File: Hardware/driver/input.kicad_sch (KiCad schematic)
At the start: 63 parts, among them J301 1017526, Q301 IXTH80N075L2, Q302 IXTH80N075L2, U301 MCP3421A2T-ECH, U302 MCP3421A1T-ECH, U303 DAC60501Z, U304 DAC60501Z, U305 DS18B20, U306 DS18B20, U307 MCP3421A3T-ECH, U308 OPA2388, U309 OPA2388, U310 LM431SC, U311 LM431SC

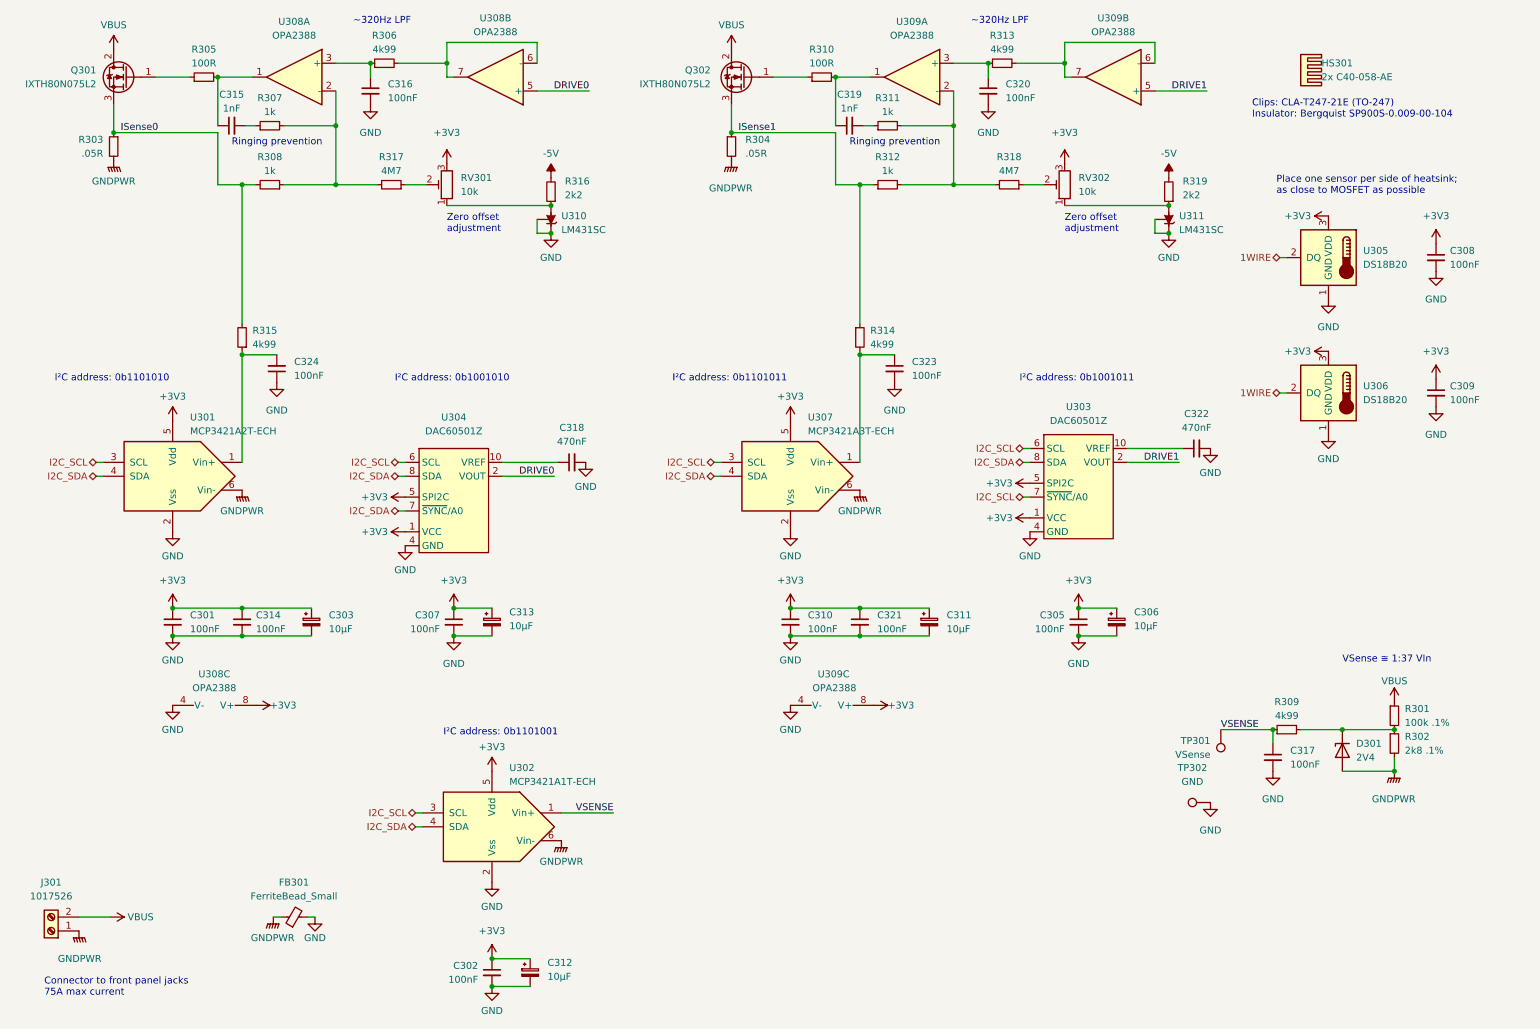
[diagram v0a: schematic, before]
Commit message: Start work on remote VSense; driver board tweaks
- Use the DAC reference as the positive end of the null adjustment
  trimmers, rather than the +3V3 supply; this should make the adjustment
  actually useful and persistent rather than relying on the relationship
  between the 3V3 rail and the DAC's internal reference.

- Moved the 1Wire controller slightly to allow relocating the zero
  offset trimmer for the first channel

- Start work on remote VSense

  This works by selecting between either voltage sensing at the source
  terminals, or an external sense input connected to another set of
  terminals. These are switched by a latching relay (as to provide
  satisfying clicky noises) and then go into an op amp working as a
  differential amplifier; it performs a 50:1 gain (obviating the need
  for resistor dividers, and providing greater accuracy) and that then
  goes into the measurement ADC as normal.

  We have to still figure out how to drive the relay (probably just an
  IO expander?) and place those components on the board.
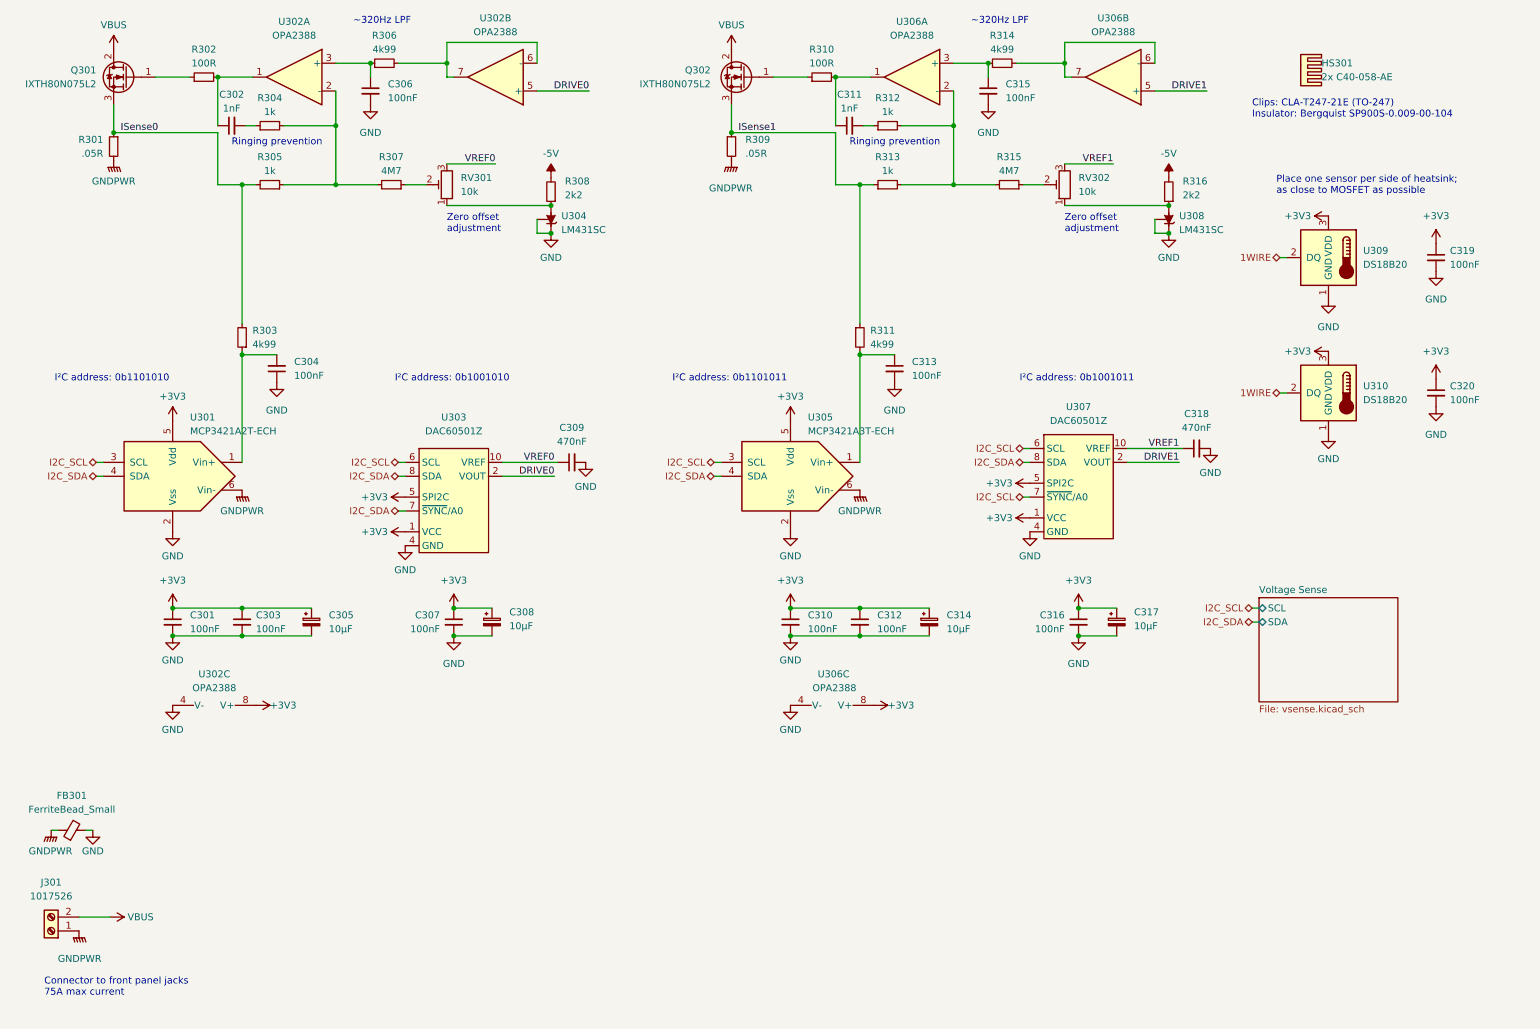
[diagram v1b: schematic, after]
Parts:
- removed C302, C317: 100nF, Capacitor_SMD:C_0805_2012Metric_Pad1.18x1.45mm_HandSolder, symbol Device:C_Small
- removed C312: 10µF, Capacitor_Tantalum_SMD:CP_EIA-3216-18_Kemet-A_Pad1.58x1.35mm_HandSolder, symbol Device:C_Polarized_Small
- removed D301: 2V4, Diode_SMD:D_MiniMELF_Handsoldering, symbol Device:D_Zener
- removed R301: 100k .1%, Resistor_SMD:R_1206_3216Metric_Pad1.30x1.75mm_HandSolder, symbol Device:R_Small
- removed R302: 2k8 .1%, Resistor_SMD:R_1206_3216Metric_Pad1.30x1.75mm_HandSolder, symbol Device:R_Small
- removed R309: 4k99, Resistor_SMD:R_0805_2012Metric_Pad1.20x1.40mm_HandSolder, symbol Device:R_Small
- removed TP301: VSense, TestPoint:TestPoint_Keystone_5000-5004_Miniature, symbol Connector:TestPoint
- removed TP302: GND, TestPoint:TestPoint_Keystone_5000-5004_Miniature, symbol Connector:TestPoint
- removed U302: MCP3421A1T-ECH, Package_TO_SOT_SMD:SOT-23-6_Handsoldering, symbol Analog_ADC:MCP3421A0T-ECH
- renumbered C315 to C302, C314 to C303, C324 to C304, C303 to C305, C316 to C306, C313 to C308, C318 to C309, C319 to C311, C321 to C312, C323 to C313, C311 to C314, C320 to C315, C305 to C316, C306 to C317, C322 to C318, C308 to C319, C309 to C320, R303 to R301, R305 to R302, R315 to R303, R307 to R304, R308 to R305, R317 to R307, R316 to R308, R304 to R309, R314 to R311, R311 to R312, R312 to R313, R313 to R314, R318 to R315, R319 to R316, U308 to U302, U304 to U303, U310 to U304, U307 to U305, U309 to U306, U303 to U307, U311 to U308, U305 to U309, U306 to U310
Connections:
- net +3V3: no longer RV301.3, RV302.3
- net VREF1: now reaches C318.1, U307.10 (VREF)
- net VREF1: now also RV302.3
- net VREF0: now reaches C309.1, U303.10 (VREF)
- net VREF0: now also RV301.3
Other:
- added sheet Voltage Sense (vsense.kicad_sch)
- note removed: "I²C address: 0b1101001"
- note removed: "VSense ≅ 1:37 VIn"
- moved on the sheet: FB301

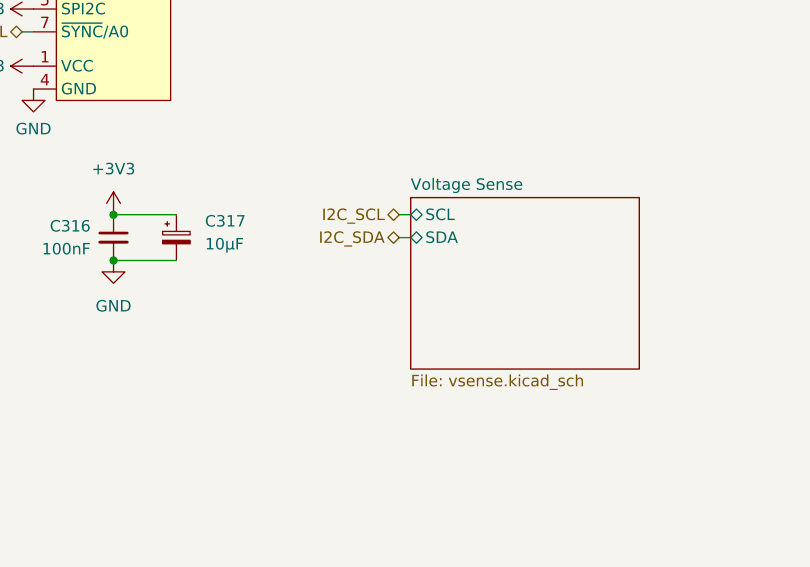
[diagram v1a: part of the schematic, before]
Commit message: Finished remote VSense support
- Laid out the VSense amp and analog-to-digital converter, as well as
  added an I2C IO expander to handle driving the latching relay to
  switch between internal and external sense.

  Also moved the input connector and some of the analog parts around to
  accomodate this all.

- Status indicator (with an extra GPIO on the IO expander) in the form
  of a single LED
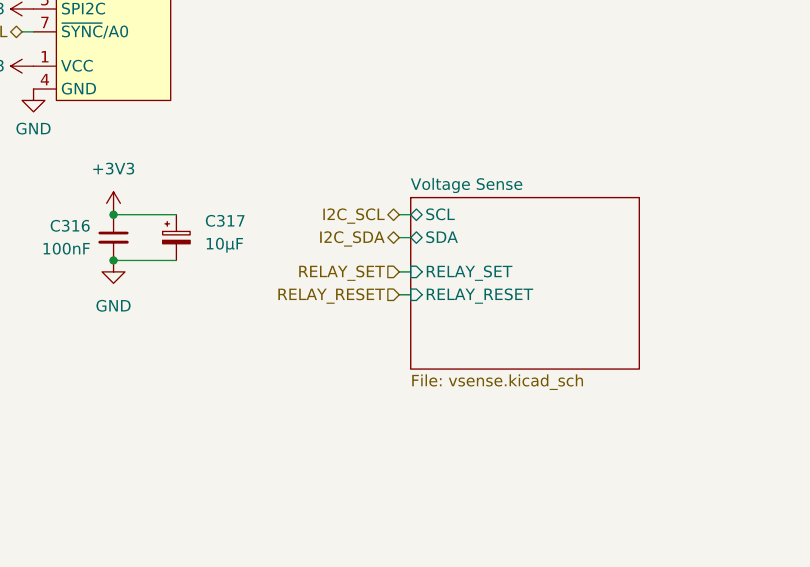
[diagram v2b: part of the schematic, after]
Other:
- sheet Voltage Sense ports: added RELAY_RESET, RELAY_SET; removed none
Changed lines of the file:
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@@
     (comment 1 "Isense options: .1R (Johanson Dielectrics RHXH3N000R1F4), .05R (Ohmite AP101 R05 J)")
     (comment 2 "Drive DACs (U303, U304) can be DAC70501Z or DAC80501Z")
+    (comment 3 "RV301, RV302 adjust current null offset")
   )
   (junction (at 155.575 127.635) (diameter 0) (color 0 0 0 0)
@@
     (stroke (width 0) (type default) (color 0 0 0 0))
   )
+  (wire (pts (xy 240.03 131.445) (xy 241.3 131.445))
+    (stroke (width 0) (type default) (color 0 0 0 0))
+  )
   (wire (pts (xy 111.76 53.975) (xy 109.22 53.975))
     (stroke (width 0) (type default) (color 0 0 0 0))
@@
   )
   (wire (pts (xy 163.83 35.56) (xy 163.83 45.085))
+    (stroke (width 0) (type default) (color 0 0 0 0))
+  )
+  (wire (pts (xy 240.03 128.905) (xy 241.3 128.905))
     (stroke (width 0) (type default) (color 0 0 0 0))
   )
@@
     (effects (font (size 1.27 1.27)) (justify right))
   )
+  (hierarchical_label "RELAY_RESET" (shape input) (at 240.03 131.445 180)
+    (effects (font (size 1.27 1.27)) (justify right))
+  )
   (hierarchical_label "I2C_SCL" (shape bidirectional) (at 240.03 122.555 180)
     (effects (font (size 1.27 1.27)) (justify right))
@@
   )
   (hierarchical_label "I2C_SCL" (shape bidirectional) (at 141.605 95.885 180)
+    (effects (font (size 1.27 1.27)) (justify right))
+  )
+  (hierarchical_label "RELAY_SET" (shape input) (at 240.03 128.905 180)
     (effects (font (size 1.27 1.27)) (justify right))
   )
@@
       (effects (font (size 1.27 1.27)) (justify left))
     )
+    (pin "RELAY_SET" input (at 241.3 128.905 180)
+      (effects (font (size 1.27 1.27)) (justify left))
+    )
+    (pin "RELAY_RESET" input (at 241.3 131.445 180)
+      (effects (font (size 1.27 1.27)) (justify left))
+    )

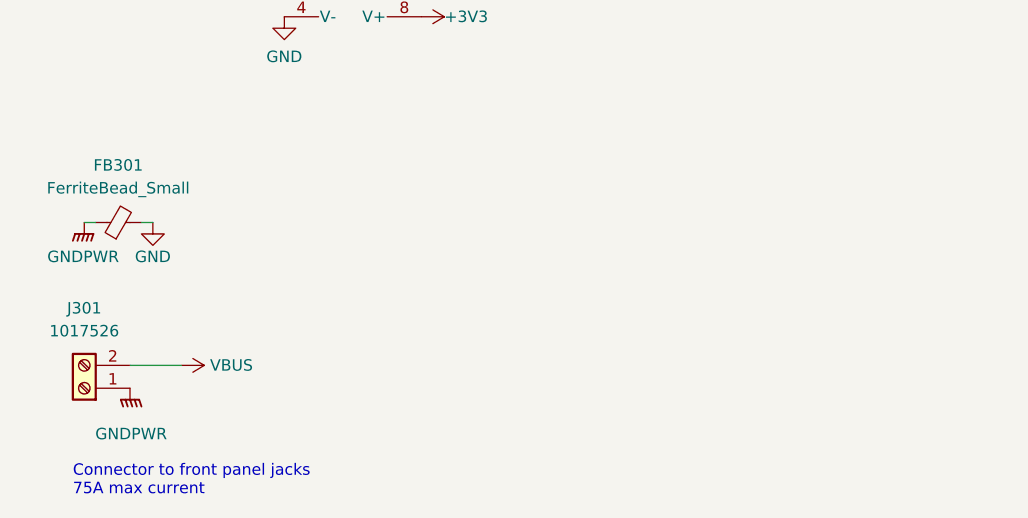
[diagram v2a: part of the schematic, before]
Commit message: Driver input protection; heatsink footprint tweaks
- Updated the footprint for the heatsink on the driver board to include
  a 3D model. Also fixed it… the distances were kind of out of whack and
  it would never have really fit

- Added a reverse polarity protection diode to the input; it gets its
  own cute little heatsink

- Minor movement to better accomodate a fan. A 20mm fan will likely
  interfere with the input connector (it might be worth switching to a
  different kind, or just soldering the connections altogether: spade
  terminals seem like a good choice for high current) and be very tight
  against the input diode's heatsink. We'll try with a 10mm fan and see
  if that's enough airflow.
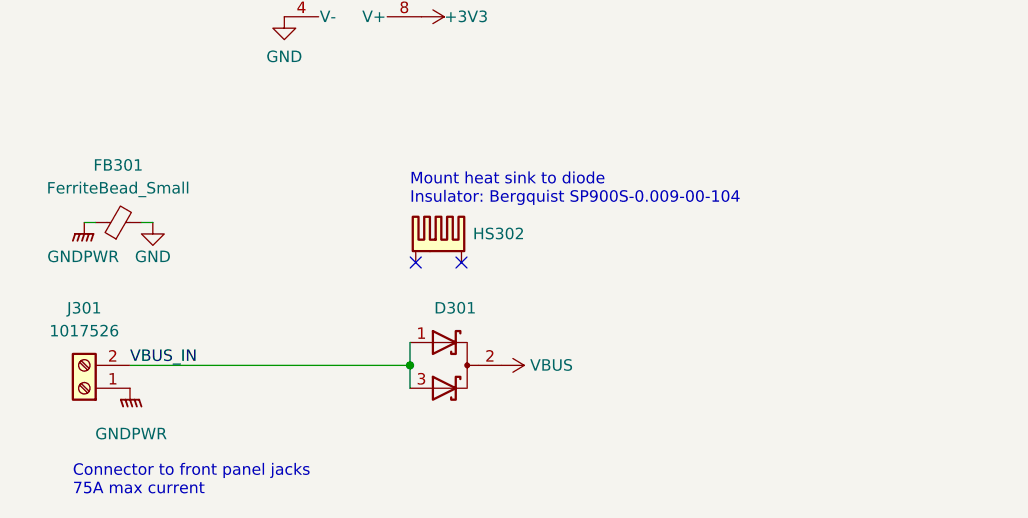
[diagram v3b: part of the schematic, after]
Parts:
- added D301: DSA120C150QB, Package_TO_SOT_THT:TO-247-3_Vertical, symbol Device:D_Schottky_Dual_CommonCathode_AKA_Parallel
- added HS302: WV-T247-101E, programmable-load:Ohmite-WA-T247-101E-MFG, symbol Mechanical:Heatsink_Pad_2Pin
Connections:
- net VBUS: now also D301.2 (A); no longer J301.2 (Pin_2)
- new net VBUS_IN: D301.1 (K), D301.3 (K), J301.2 (Pin_2)
- no-connect marks 0 -> 2
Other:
- note added: "Mount heat sink to diode Insulator: Bergquist SP900S-0.009-00-104"
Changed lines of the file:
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@@
   (junction (at 168.275 127.635) (diameter 0) (color 0 0 0 0)
   )
+  (junction (at 56.515 179.07) (diameter 0) (color 0 0 0 0)
+  )
   (junction (at 55.245 122.555) (diameter 0) (color 0 0 0 0)
   )
@@
   (junction (at 72.39 34.29) (diameter 0) (color 0 0 0 0)
   )
+  (no_connect (at 57.15 167.64))
+  (no_connect (at 62.23 167.64))
   (wire (pts (xy 50.8 45.085) (xy 55.245 45.085))
     (stroke (width 0) (type default) (color 0 0 0 0))
@@
     (stroke (width 0) (type default) (color 0 0 0 0))
   )
+  (wire (pts (xy 56.515 179.07) (xy 56.515 181.61))
+    (stroke (width 0) (type default) (color 0 0 0 0))
+  )
   (wire (pts (xy 168.275 45.085) (xy 170.815 45.085))
     (stroke (width 0) (type default) (color 0 0 0 0))
@@
     (stroke (width 0) (type default) (color 0 0 0 0))
   )
-  (wire (pts (xy 31.115 179.07) (xy 25.4 179.07))
+  (wire (pts (xy 25.4 179.07) (xy 56.515 179.07))
     (stroke (width 0) (type default) (color 0 0 0 0))
   )
@@
   )
   (wire (pts (xy 217.17 93.345) (xy 227.33 93.345))
+    (stroke (width 0) (type default) (color 0 0 0 0))
+  )
+  (wire (pts (xy 56.515 179.07) (xy 56.515 176.53))
     (stroke (width 0) (type default) (color 0 0 0 0))
   )
@@
     (effects (font (size 1.27 1.27)) (justify left bottom))
   )
+  (text "Mount heat sink to diode\nInsulator: Bergquist SP900S-0.009-00-104"
+    (at 56.515 161.29 0)
+    (effects (font (size 1.27 1.27)) (justify left bottom))
+  )
   (label "DRIVE1" (at 231.775 27.94 180)
     (effects (font (size 1.27 1.27)) (justify right bottom))
@@
   )
   (label "ISense0" (at 33.02 35.56 0)
+    (effects (font (size 1.27 1.27)) (justify left bottom))
+  )
+  (label "VBUS_IN" (at 25.4 179.07 0)
     (effects (font (size 1.27 1.27)) (justify left bottom))
   )
@@
     (pin "2")
   )
+  (symbol (lib_id "Device:D_Schottky_Dual_CommonCathode_AKA_Parallel") (at 61.595 179.07 0) (unit 1)
+    (in_bom yes) (on_board yes) (fields_autoplaced)
+    (property "Reference" "D301" (id 0) (at 61.5315 172.72 0))
+    (property "Value" "DSA120C150QB" (id 1) (at 61.5315 172.085 0)
+      (effects (font (size 1.27 1.27)) hide)
+    )
+    (property "Footprint" "Package_TO_SOT_THT:TO-247-3_Vertical" (id 2) (at 62.865 179.07 0)
+      (effects (font (size 1.27 1.27)) hide)
+    )
+    (property "Datasheet" "~" (id 3) (at 62.865 179.07 0)
+      (effects (font (size 1.27 1.27)) hide)
+    )
+    (property "MPN" "DSA120C150QB" (id 4) (at 61.595 179.07 0)
+      (effects (font (size 1.27 1.27)) hide)
+    )
+    (pin "1")
+    (pin "2")
+    (pin "3")
+  )
   (symbol (lib_id "Device:C_Small") (at 174.625 78.74 0) (unit 1)
     (in_bom yes) (on_board yes) (fields_autoplaced)
@@
     )
     (pin "1")
+  )
+  (symbol (lib_id "Mechanical:Heatsink_Pad_2Pin") (at 59.69 165.1 0) (unit 1)
+    (in_bom yes) (on_board yes) (fields_autoplaced)
+    (property "Reference" "HS302" (id 0) (at 63.5 164.4649 0)
+      (effects (font (size 1.27 1.27)) (justify left))
+    )
+    (property "Value" "WV-T247-101E" (id 1) (at 63.5 165.7349 0)
+      (effects (font (size 1.27 1.27)) (justify left) hide)
+    )
+    (property "Footprint" "programmable-load:Ohmite-WA-T247-101E-MFG" (id 2) (at 59.9948 166.37 0)
+      (effects (font (size 1.27 1.27)) hide)
+    )
+    (property "Datasheet" "https://www.ohmite.com/assets/docs/sink_w.pdf" (id 3) (at 59.9948 166.37 0)
+      (effects (font (size 1.27 1.27)) hide)
+    )
+    (property "MPN" "WV-T247-101E" (id 4) (at 59.69 165.1 0)
+      (effects (font (size 1.27 1.27)) hide)
+    )
+    (pin "1")
+    (pin "2")
   )
   (symbol (lib_id "power:+3V3") (at 273.685 55.88 0) (mirror y) (unit 1)
@@
     (pin "1")
   )
-  (symbol (lib_id "power:VBUS") (at 31.115 179.07 270) (mirror x) (unit 1)
-    (in_bom yes) (on_board yes) (fields_autoplaced)
-    (property "Reference" "#PWR0304" (id 0) (at 27.305 179.07 0)
-      (effects (font (size 1.27 1.27)) hide)
-    )
-    (property "Value" "VBUS" (id 1) (at 34.29 179.0699 90)
-      (effects (font (size 1.27 1.27)) (justify left))
-    )
-    (property "Footprint" "" (id 2) (at 31.115 179.07 0)
-      (effects (font (size 1.27 1.27)) hide)
-    )
-    (property "Datasheet" "" (id 3) (at 31.115 179.07 0)
-      (effects (font (size 1.27 1.27)) hide)
-    )
+  (symbol (lib_id "power:VBUS") (at 66.675 179.07 270) (mirror x) (unit 1)
+    (in_bom yes) (on_board yes) (fields_autoplaced)
+    (property "Reference" "#PWR0304" (id 0) (at 62.865 179.07 0)
+      (effects (font (size 1.27 1.27)) hide)
+    )
+    (property "Value" "VBUS" (id 1) (at 69.85 179.0699 90)
+      (effects (font (size 1.27 1.27)) (justify left))
+    )
+    (property "Footprint" "" (id 2) (at 66.675 179.07 0)
+      (effects (font (size 1.27 1.27)) hide)
+    )
+    (property "Datasheet" "" (id 3) (at 66.675 179.07 0)
+      (effects (font (size 1.27 1.27)) hide)
+    )
